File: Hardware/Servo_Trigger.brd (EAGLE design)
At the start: 20.3 x 40.6 mm, 19 parts, among them Q1 16MHz, U1 ATTINY84

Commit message: PCB Work in progress
Routed board, set up basic jumpers.
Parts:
- added R5, R6: 10k, SparkFun-Passives:0402-RES
- added SJ1, SJ2: N.O., SparkFun-Passives:PAD-JUMPER-2-NO_YES_SILK
- JP1, JP3: value M02PTH -> M021X02_NO_SILK; device SparkFun-Connectors:1X02 -> SparkFun-Connectors:1X02_NO_SILK
- JP2: device SparkFun-Connectors:1X03 -> SparkFun-Connectors:1X03_NO_SILK
- R1, R2, R3: value TRIMPOTRES-11156 -> 10k
- moved C3 21.7 mm to (3.81, 31.8), turned to 0 degrees
- moved JP1 13.3 mm to (19.1, 14.0), turned to 90 degrees
- moved JP2 7.73 mm to (19.1, 31.8), turned to 90 degrees
- moved R4 5.99 mm to (1.27, 6.35), turned to 90 degrees
- moved JP9 5.08 mm to (16.5, 7.62)
- moved C2 4.02 mm to (11.4, 2.54), turned to 90 degrees
- moved C4 4.02 mm to (3.81, 2.54), turned to 270 degrees
- moved Q1 4.02 mm to (7.62, 2.54)
- moved LOGO2 3.86 mm to (8.26, 29.2)
- moved LOGO1 3.83 mm to (9.91, 34.3), turned to 270 degrees
- moved C1 2.84 mm to (1.27, 12.7)
- moved JP3 2.84 mm to (1.27, 36.8), turned to 270 degrees
- moved U1 1.80 mm to (7.62, 11.4)
- moved FID2 1.00 mm to (19.3, 29.5)
- moved R1 1.00 mm to (3.81, 21.9)
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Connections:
- new net MODESEL: R5.1, SJ1.2, U1.5
- new net POLSEL: R6.1, SJ2.2, U1.11
- net GND: now also SJ1.1, SJ2.1
- net VCC: now also R5.2, R6.2
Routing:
- net VCC: track 0.00 -> 94.4 mm
- net MOSI/PWM: track 0.00 -> 47.8 mm, vias 0 -> 1
- net T: track 0.00 -> 36.3 mm, vias 0 -> 2
- net MODESEL: track 0.00 -> 31.1 mm, vias 0 -> 1
- net POLSEL: track 0.00 -> 29.4 mm, vias 0 -> 1
- net A: track 0.00 -> 26.2 mm, vias 0 -> 2
- net RESET: track 0.00 -> 22.0 mm, vias 0 -> 2
- net B: track 0.00 -> 20.3 mm, vias 0 -> 2
- net BTN: track 0.00 -> 16.5 mm, vias 0 -> 1
- net SCK: track 0.00 -> 14.9 mm, vias 0 -> 2
- net MISO: track 0.00 -> 11.3 mm, vias 0 -> 1
- net N$3: track 0.00 -> 10.1 mm
- net N$4: track 0.00 -> 9.09 mm
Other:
- board size 20.3 x 40.6 mm -> 20.3 x 38.4 mm
- board text added: "BLK"
- board text added: "BRN"
- board text added: "ORG"
- board text added: "RED"
- board text added: "SJ1-Mode"
- board text added: "SJ2-Input Polarity"
- board text added: "SW"
- board text added: "WHT"
- board text removed: "SW IN"

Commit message: PCB updates
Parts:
- JP2: value (none) -> SERVO-OUT
- moved JP9 6.25 mm to (14.0, 1.91), turned to 0 degrees
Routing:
- net VCC: track 94.4 -> 100.2 mm
- net MISO: track 11.3 -> 15.1 mm
- net RESET: track 22.0 -> 25.6 mm
- net SCK: track 14.9 -> 17.8 mm, vias 2 -> 3
- net MODESEL: track 31.1 -> 30.1 mm
- net MOSI/PWM: track 47.8 -> 47.9 mm, vias 1 -> 2
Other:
- board size 20.3 x 38.4 mm -> 20.3 x 38.1 mm

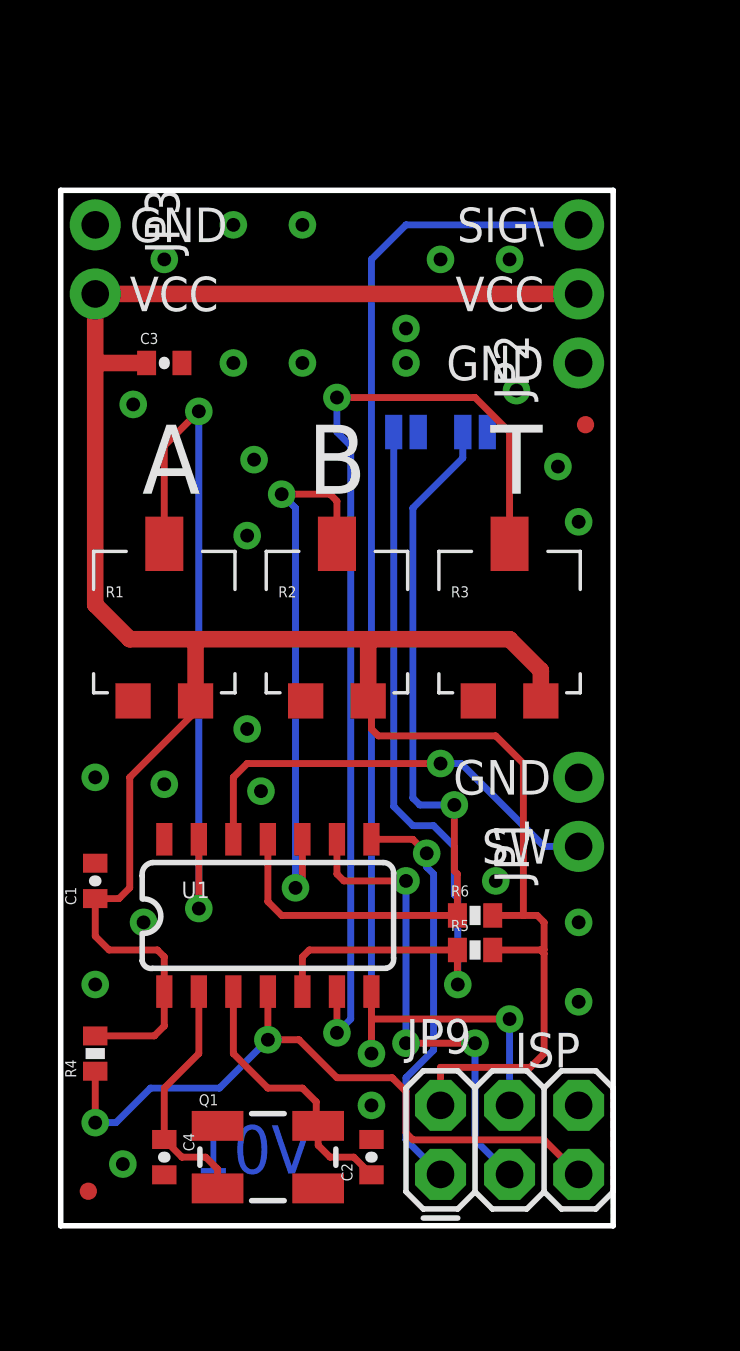
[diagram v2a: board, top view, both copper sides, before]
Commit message: Updating parts
I'd cut & pasted the tiny programmer, which used outdated parts.

Updated to 0603 resistors & caps, using resonator instead of crystal,
etc.
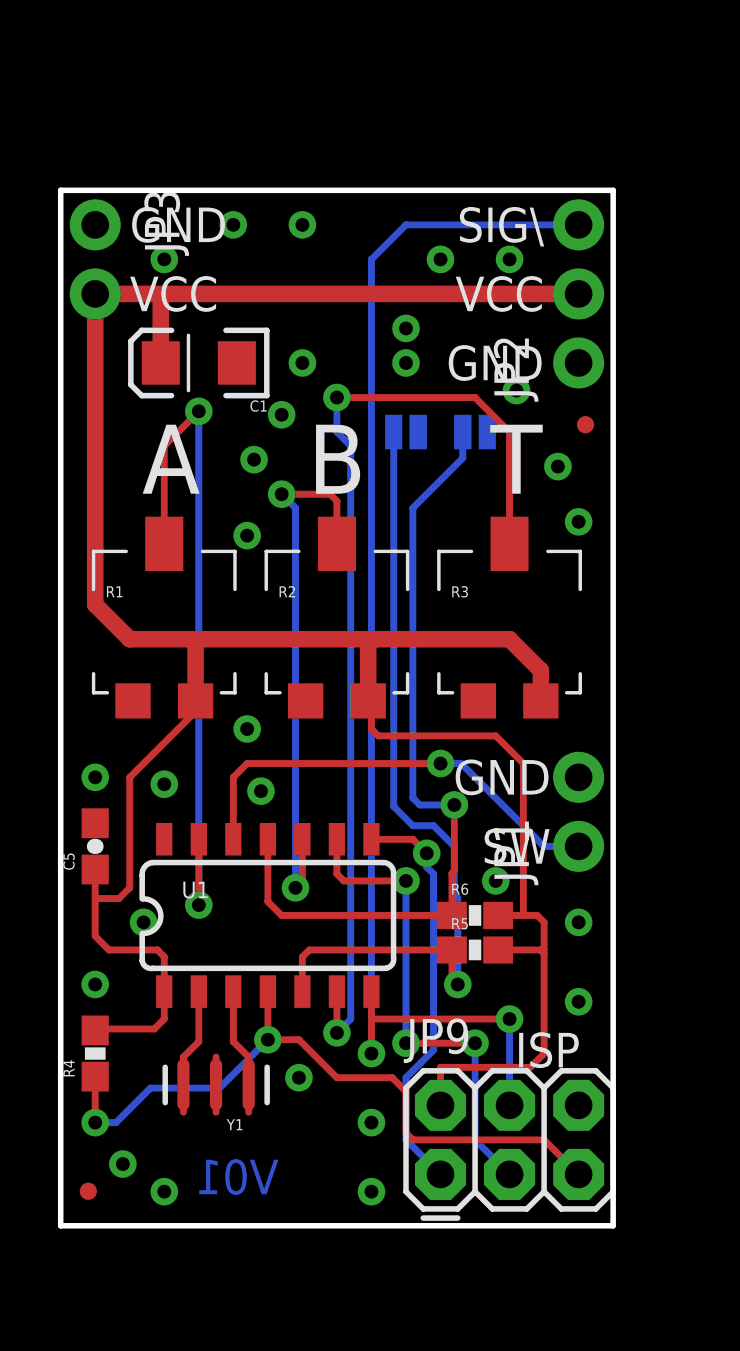
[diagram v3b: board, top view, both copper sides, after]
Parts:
- removed C2, C4: 18pF, SparkFun-Passives:0402-CAP
- removed C3: 10uF, SparkFun-Passives:0402-CAP
- removed Q1: 16MHz, SparkFun-FreqCtrl:CRYSTAL-SMD-5X3
- added C5: 0.1uF, SparkFun-Capacitors:0603-CAP
- added Y1: 16MHZ, SparkFun-FreqCtrl:RESONATOR-SMD
- C1: value 0.1uF -> 10uF; device SparkFun-Passives:0402-CAP -> SparkFun-Capacitors:EIA3216
- R4, R5, R6: device SparkFun-Passives:0402-RES -> SparkFun-Resistors:0603-RES
- moved C1 19.4 mm to (5.08, 31.8), turned to 180 degrees
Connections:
- net GND: now also C1.C, C5.2, Y1.2; no longer C1.2, C2.2, C3.2, C4.2
- net N$3: now also Y1.1; no longer C2.1, Q1.3
- net N$4: now also Y1.3; no longer C4.1, Q1.1
- net VCC: now also C1.A, C5.1; no longer C1.1, C3.1
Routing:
- net N$3: track 10.1 -> 2.64 mm
- net N$4: track 9.09 -> 2.64 mm
- net VCC: track 100.2 -> 101.3 mm

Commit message: More WIP.
Added one-shot FSM.
Cleaned up gratuitous magic constants.
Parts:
- moved C5 2.54 mm to (1.27, 11.4), turned to 270 degrees
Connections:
- net GND: now also R1.A, R2.A, R3.A; no longer R1.C, R2.C, R3.C
- net VCC: now also R1.C, R2.C, R3.C; no longer R1.A, R2.A, R3.A
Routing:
- net VCC: track 101.3 -> 93.9 mm
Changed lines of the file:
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@@
 <text x="21.082" y="34.29" size="1.27" layer="51" font="vector" ratio="15" align="center-left">RED</text>
 <text x="21.082" y="36.83" size="1.27" layer="51" font="vector" ratio="15" align="center-left">WHT</text>
-<text x="28.702" y="31.75" size="1.27" layer="51" font="vector" ratio="15" align="center-left">BRN</text>
-<text x="28.702" y="36.83" size="1.27" layer="51" font="vector" ratio="15" align="center-left">ORG</text>
-<text x="28.702" y="34.29" size="1.27" layer="51" font="vector" ratio="15" align="center-left">RED</text>
+<text x="26.162" y="31.75" size="1.27" layer="51" font="vector" ratio="15" align="center-left">BRN</text>
+<text x="26.162" y="36.83" size="1.27" layer="51" font="vector" ratio="15" align="center-left">ORG</text>
+<text x="26.162" y="34.29" size="1.27" layer="51" font="vector" ratio="15" align="center-left">RED</text>
 <dimension x1="0" y1="0.016" x2="0" y2="38.1" x3="-6.35" y3="19.058" textsize="1.778" textratio="15" layer="51" unit="inch" visible="yes"/>
 <dimension x1="0" y1="38.1" x2="20.32" y2="38.1" x3="10.16" y3="45.72" textsize="1.778" textratio="15" layer="51" unit="inch" visible="yes"/>
@@
 <element name="SJ1" library="SparkFun-Passives" package="PAD-JUMPER-2-NO_YES_SILK" value="N.O." x="12.7" y="29.21" rot="MR0"/>
 <element name="SJ2" library="SparkFun-Passives" package="PAD-JUMPER-2-NO_YES_SILK" value="N.O." x="15.24" y="29.21" rot="MR0"/>
-<element name="C5" library="SparkFun-Capacitors" package="0603-CAP" value="0.1uF" x="1.27" y="13.97" rot="R90">
-<attribute name="PROD_ID" value="CAP-00810" x="1.27" y="13.97" size="1.778" layer="27" font="vector" ratio="15" rot="R90" display="off"/>
+<element name="C5" library="SparkFun-Capacitors" package="0603-CAP" value="0.1uF" x="1.27" y="11.43" rot="R270">
+<attribute name="PROD_ID" value="CAP-00810" x="1.27" y="11.43" size="1.778" layer="27" font="vector" ratio="15" rot="R270" display="off"/>
 </element>
 <element name="C1" library="SparkFun-Capacitors" package="EIA3216" value="10uF" x="5.08" y="31.75" rot="R180">
@@
 <contactref element="U1" pad="1"/>
 <contactref element="R4" pad="2"/>
-<contactref element="R3" pad="A"/>
-<contactref element="R2" pad="A"/>
-<contactref element="R1" pad="A"/>
 <contactref element="JP2" pad="2"/>
 <contactref element="JP3" pad="2"/>
 <contactref element="R5" pad="2"/>
 <contactref element="R6" pad="2"/>
-<wire x1="1.27" y1="34.29" x2="1.27" y2="22.86" width="0.6096" layer="1"/>
-<wire x1="1.27" y1="22.86" x2="2.54" y2="21.59" width="0.6096" layer="1"/>
-<wire x1="2.54" y1="21.59" x2="5.08" y2="21.59" width="0.6096" layer="1"/>
-<wire x1="5.08" y1="21.59" x2="11.43" y2="21.59" width="0.6096" layer="1"/>
-<wire x1="11.43" y1="21.59" x2="16.51" y2="21.59" width="0.6096" layer="1"/>
-<wire x1="17.66" y1="19.32" x2="17.66" y2="20.44" width="0.6096" layer="1"/>
-<wire x1="17.66" y1="20.44" x2="16.51" y2="21.59" width="0.6096" layer="1"/>
-<wire x1="11.31" y1="19.32" x2="11.31" y2="21.47" width="0.6096" layer="1"/>
-<wire x1="11.31" y1="21.47" x2="11.43" y2="21.59" width="0.6096" layer="1"/>
-<wire x1="4.96" y1="19.32" x2="4.96" y2="21.47" width="0.6096" layer="1"/>
+<wire x1="1.27" y1="34.29" x2="1.27" y2="21.59" width="0.6096" layer="1"/>
+<wire x1="1.27" y1="21.59" x2="5.08" y2="21.59" width="0.6096" layer="1"/>
+<wire x1="5.08" y1="21.59" x2="8.89" y2="21.59" width="0.6096" layer="1"/>
+<wire x1="8.89" y1="21.59" x2="14.605" y2="21.59" width="0.6096" layer="1"/>
 <wire x1="4.96" y1="21.47" x2="5.08" y2="21.59" width="0.6096" layer="1"/>
 <wire x1="3.81" y1="8.63" x2="3.81" y2="7.62" width="0.254" layer="1"/>
 <wire x1="3.444" y1="7.254" x2="3.81" y2="7.62" width="0.254" layer="1"/>
-<wire x1="3.81" y1="8.63" x2="3.81" y2="9.906" width="0.254" layer="1"/>
-<wire x1="3.81" y1="9.906" x2="3.556" y2="10.16" width="0.254" layer="1"/>
-<wire x1="3.556" y1="10.16" x2="1.778" y2="10.16" width="0.254" layer="1"/>
-<wire x1="1.778" y1="10.16" x2="1.27" y2="10.668" width="0.254" layer="1"/>
-<wire x1="4.96" y1="19.32" x2="4.96" y2="18.93" width="0.254" layer="1"/>
-<wire x1="4.96" y1="18.93" x2="2.54" y2="16.51" width="0.254" layer="1"/>
-<wire x1="2.54" y1="16.51" x2="2.54" y2="12.446" width="0.254" layer="1"/>
-<wire x1="2.144" y1="12.05" x2="2.54" y2="12.446" width="0.254" layer="1"/>
+<wire x1="3.81" y1="8.63" x2="3.81" y2="9.906" width="0.3048" layer="1"/>
+<wire x1="3.81" y1="9.906" x2="3.556" y2="10.16" width="0.3048" layer="1"/>
+<wire x1="3.556" y1="10.16" x2="3.048" y2="10.16" width="0.3048" layer="1"/>
+<wire x1="3.048" y1="10.16" x2="2.54" y2="10.668" width="0.3048" layer="1"/>
 <wire x1="19.05" y1="34.29" x2="3.81" y2="34.29" width="0.6096" layer="1"/>
 <wire x1="3.81" y1="34.29" x2="1.27" y2="34.29" width="0.6096" layer="1"/>
@@
 <wire x1="17.526" y1="11.43" x2="17.78" y2="11.176" width="0.254" layer="1"/>
 <wire x1="17.78" y1="10.16" x2="17.78" y2="11.176" width="0.254" layer="1"/>
-<wire x1="17.78" y1="19.2" x2="17.66" y2="19.32" width="0.254" layer="1"/>
-<wire x1="17.018" y1="11.43" x2="17.018" y2="17.018" width="0.254" layer="1"/>
-<wire x1="17.018" y1="17.018" x2="16.002" y2="18.034" width="0.254" layer="1"/>
-<wire x1="16.002" y1="18.034" x2="11.684" y2="18.034" width="0.254" layer="1"/>
-<wire x1="11.684" y1="18.034" x2="11.43" y2="18.288" width="0.254" layer="1"/>
-<wire x1="11.43" y1="18.288" x2="11.43" y2="19.2" width="0.254" layer="1"/>
-<wire x1="11.43" y1="19.2" x2="11.31" y2="19.32" width="0.254" layer="1"/>
+<wire x1="17.018" y1="11.43" x2="17.018" y2="16.51" width="0.254" layer="1"/>
+<wire x1="17.018" y1="16.51" x2="15.36" y2="18.168" width="0.254" layer="1"/>
 <wire x1="13.97" y1="4.445" x2="13.97" y2="5.842" width="0.254" layer="1"/>
 <wire x1="13.97" y1="5.842" x2="17.272" y2="5.842" width="0.254" layer="1"/>
@@
 <contactref element="C5" pad="1"/>
 <contactref element="C1" pad="A"/>
-<wire x1="1.27" y1="13.12" x2="1.27" y2="12.065" width="0.254" layer="1"/>
-<wire x1="1.27" y1="12.065" x2="1.27" y2="10.668" width="0.254" layer="1"/>
-<wire x1="2.144" y1="12.05" x2="1.285" y2="12.05" width="0.254" layer="1"/>
-<wire x1="1.285" y1="12.05" x2="1.27" y2="12.065" width="0.254" layer="1"/>
+<wire x1="2.54" y1="12.065" x2="2.54" y2="10.668" width="0.3048" layer="1"/>
 <wire x1="3.68" y1="31.75" x2="3.68" y2="34.16" width="0.6096" layer="1"/>
 <wire x1="3.68" y1="34.16" x2="3.81" y2="34.29" width="0.6096" layer="1"/>
 <wire x1="3.444" y1="7.254" x2="1.324" y2="7.254" width="0.254" layer="1"/>
 <wire x1="1.324" y1="7.254" x2="1.27" y2="7.2" width="0.254" layer="1"/>
+<contactref element="R1" pad="C"/>
+<wire x1="2.66" y1="19.32" x2="1.27" y2="19.32" width="0.254" layer="1"/>
+<wire x1="1.27" y1="21.59" x2="1.27" y2="19.32" width="0.6096" layer="1"/>
+<wire x1="1.27" y1="19.32" x2="1.27" y2="12.28" width="0.6096" layer="1"/>
+<wire x1="2.54" y1="12.065" x2="2.325" y2="12.28" width="0.3048" layer="1"/>
+<wire x1="2.325" y1="12.28" x2="1.27" y2="12.28" width="0.3048" layer="1"/>
+<contactref element="R3" pad="C"/>
+<contactref element="R2" pad="C"/>
+<wire x1="15.36" y1="19.32" x2="15.36" y2="20.835" width="0.6096" layer="1"/>
+<wire x1="15.36" y1="20.835" x2="14.605" y2="21.59" width="0.6096" layer="1"/>
+<wire x1="9.01" y1="19.32" x2="9.01" y2="21.47" width="0.6096" layer="1"/>
+<wire x1="9.01" y1="21.47" x2="8.89" y2="21.59" width="0.6096" layer="1"/>
+<wire x1="15.36" y1="19.32" x2="15.36" y2="18.168" width="0.254" layer="1"/>
 </signal>
 <signal name="GND">
 <contactref element="U1" pad="14"/>
 <contactref element="JP9" pad="6"/>
-<contactref element="R1" pad="C"/>
-<contactref element="R2" pad="C"/>
-<contactref element="R3" pad="C"/>
 <contactref element="JP2" pad="1"/>
 <contactref element="JP1" pad="2"/>
@@
 <via x="1.27" y="8.89" extent="1-16" drill="0.508"/>
 <via x="2.286" y="2.286" extent="1-16" drill="0.508"/>
-<via x="1.27" y="16.51" extent="1-16" drill="0.508"/>
+<via x="2.54" y="17.78" extent="1-16" drill="0.508"/>
 <via x="3.81" y="35.56" extent="1-16" drill="0.508"/>
 <via x="6.35" y="36.83" extent="1-16" drill="0.508"/>
 <via x="16.51" y="35.56" extent="1-16" drill="0.508"/>
 <via x="8.128" y="29.845" extent="1-16" drill="0.508"/>
-<via x="3.048" y="11.176" extent="1-16" drill="0.508"/>
+<via x="2.54" y="8.89" extent="1-16" drill="0.508"/>
 <via x="19.05" y="8.255" extent="1-16" drill="0.508"/>
 <via x="19.05" y="11.176" extent="1-16" drill="0.508"/>
@@
 <via x="6.858" y="25.4" extent="1-16" drill="0.508"/>
 <via x="6.858" y="18.288" extent="1-16" drill="0.508"/>
-<via x="3.81" y="16.256" extent="1-16" drill="0.508"/>
 <via x="7.366" y="16.002" extent="1-16" drill="0.508"/>
 <via x="16.002" y="12.7" extent="1-16" drill="0.508"/>
@@
 <via x="11.43" y="1.27" extent="1-16" drill="0.508"/>
 <via x="3.81" y="1.27" extent="1-16" drill="0.508"/>
+<contactref element="R1" pad="A"/>
+<contactref element="R3" pad="A"/>
+<contactref element="R2" pad="A"/>
+<via x="2.54" y="15.24" extent="1-16" drill="0.508"/>
 </signal>
 <signal name="MOSI/PWM">
